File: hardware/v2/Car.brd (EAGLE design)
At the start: 83.8 x 55.9 mm, 80 parts, among them M1_CA 100n, M1_CB 100n, M1_LPF MCP6L2-X_SN, M1_LPF1 MCP6L2-X_SN, M1_R1A 105k, M1_R1B 105k, M1_R2A 200k, M1_R2B 200k, M1_RA 22k, M1_RB 22k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

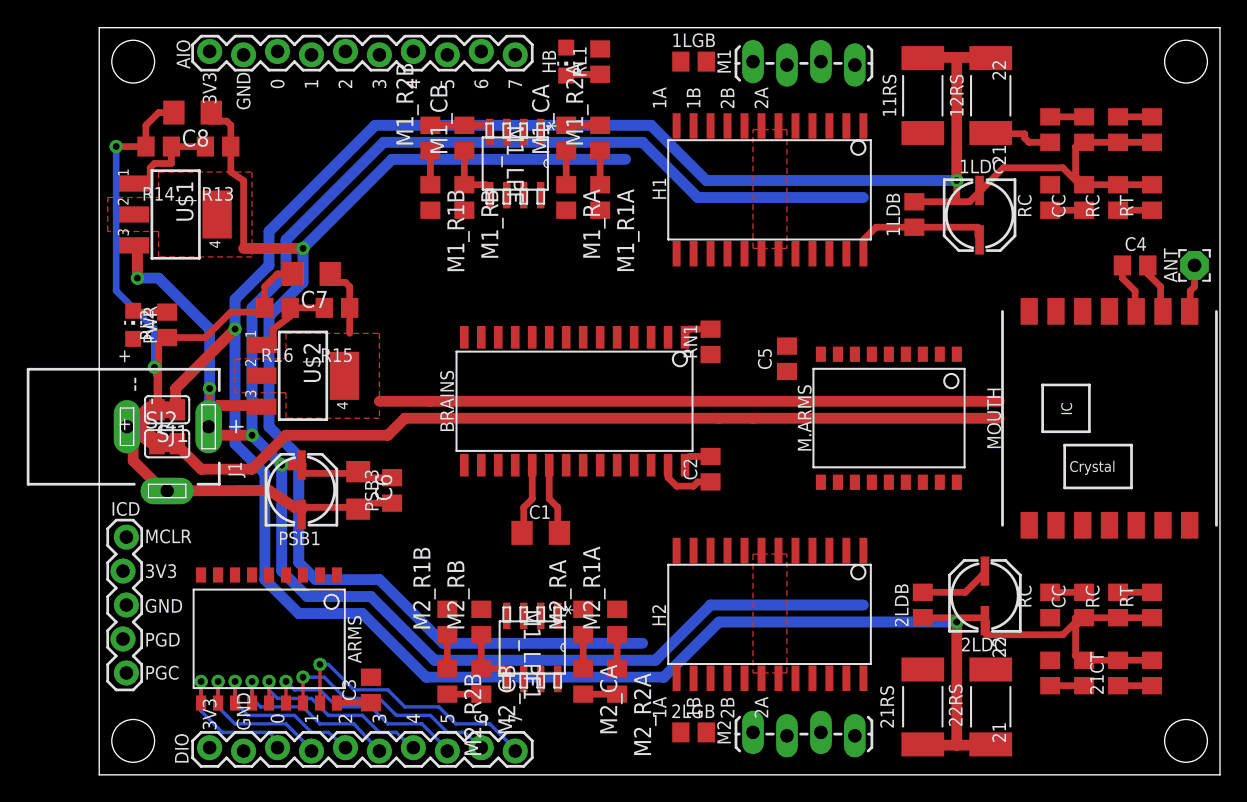
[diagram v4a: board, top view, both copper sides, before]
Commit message: Finished routing power signals.
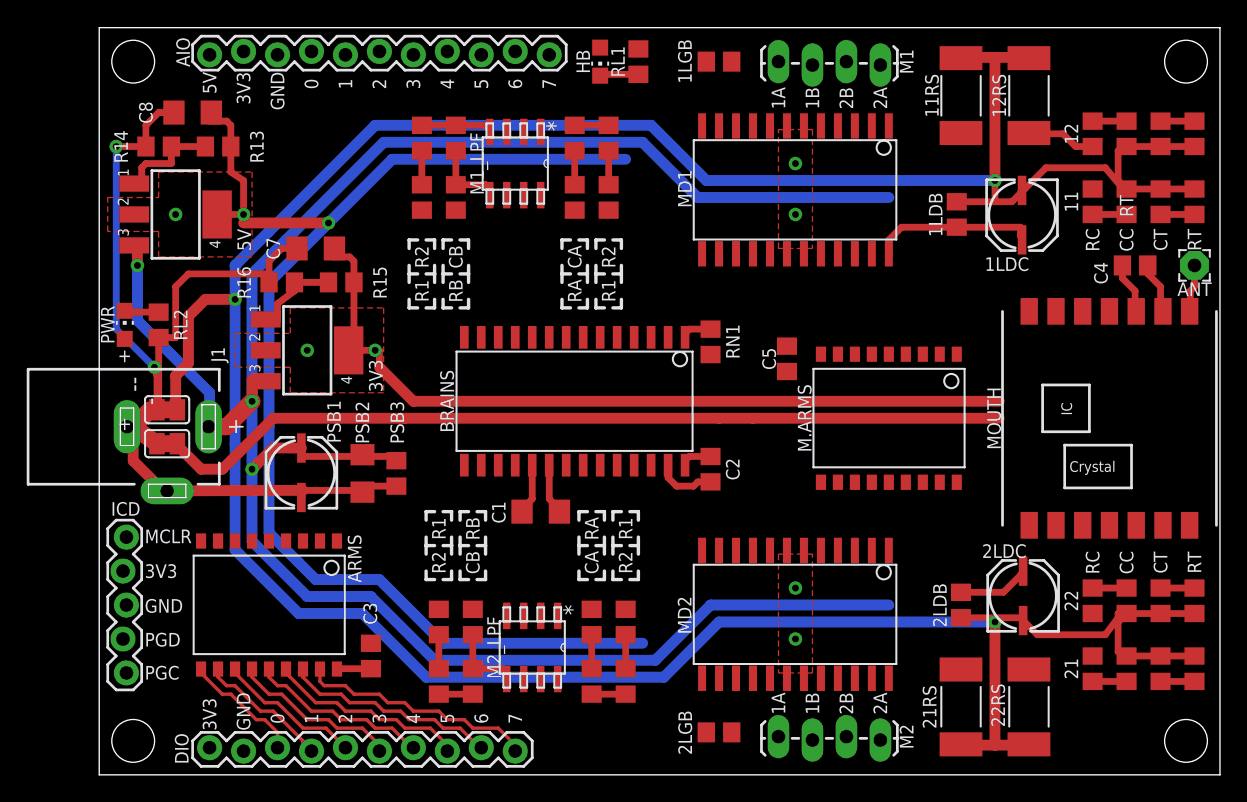
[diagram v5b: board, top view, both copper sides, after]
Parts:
- removed C6: 1u, rcl:C1206
- removed H1, H2: MTS62C19A, microchip:SOP24L
- removed U$2: LM317, misc:SOT23
- added 3V3: LM317, misc:SOT23
- added MD1, MD2: MTS62C19A, microchip:SOP24L
- added PSB2: 1u, rcl:C1206
- AIO: device SparkFun-Connectors:1X10_LOCK -> SparkFun-Connectors:1X11_LOCK
- moved AIO 25.4 mm to (33.7, 54.0), turned to 180 degrees
- moved 11RT 3.19 mm to (81.9, 42.9)
- moved 21RT 3.19 mm to (81.9, 7.94)
- moved 22RT 3.19 mm to (81.9, 13.0)
- moved 12RT 3.19 mm to (81.9, 47.9)
- moved 11CC 3.19 mm to (76.8, 42.9)
- moved 11CT 3.19 mm to (79.4, 42.9)
- moved 11RC 3.19 mm to (74.3, 42.9)
- moved 12CC 3.19 mm to (76.8, 47.9)
- moved 12CT 3.19 mm to (79.4, 47.9)
- moved 12RC 3.19 mm to (74.3, 47.9)
- moved 21CC 3.19 mm to (76.8, 7.94)
- moved 21CT 3.19 mm to (79.4, 7.94)
- moved 21RC 3.19 mm to (74.3, 7.94)
- moved 22CC 3.19 mm to (76.8, 13.0)
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- renumbered M1_LPF1 to M2_LPF, U$1 to 5V
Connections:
- net 12V: now also 3V3.3, MD1.24, MD2.24, PSB2.1; no longer C6.1, H1.24, H2.24, U$2.3
- net 3V3: now also 3V3.2, 3V3.4, AIO.10; no longer AIO.1, U$2.2, U$2.4
- net 5V: now also AIO.11, MD1.13, MD2.13; no longer H1.13, H2.13
- net A0: now also AIO.8; no longer AIO.3
- net A1: now also AIO.7; no longer AIO.4
- net A2: now also AIO.6; no longer AIO.5
- net A3: now also AIO.5; no longer AIO.6
- net A4: now also AIO.4; no longer AIO.7
- net A5: now also AIO.3; no longer AIO.8
- net A6: now also AIO.2; no longer AIO.9
- net A7: now also AIO.1; no longer AIO.10
- net DGND: now also AIO.9, MD1.18, MD1.19, MD1.6, MD1.7, MD2.18, MD2.19, MD2.6, MD2.7; no longer AIO.2, H1.18, H1.19, H1.6, H1.7, H2.18, H2.19, H2.6, H2.7
- net GND: now also PSB2.2; no longer C6.2
- net M1_I0X: now also MD1.20, MD1.8; no longer H1.20, H1.8
- net M1_I1X: now also MD1.17, MD1.9; no longer H1.17, H1.9
- net M1_P1: now also MD1.16; no longer H1.16
- net M1_P2: now also MD1.10; no longer H1.10
- net M1_V1: now also MD1.15; no longer H1.15
- net M1_V2: now also MD1.11; no longer H1.11
- net M2_I0X: now also MD2.20, MD2.8; no longer H2.20, H2.8
- net M2_I1X: now also MD2.17, MD2.9; no longer H2.17, H2.9
- net M2_P1: now also MD2.16; no longer H2.16
- net M2_P2: now also MD2.10; no longer H2.10
- net M2_V1: now also MD2.15; no longer H2.15
- net M2_V2: now also MD2.11; no longer H2.11
- net N$1: now also MD1.21; no longer H1.21
- net N$10: now also MD2.2; no longer H2.2
- net N$13: now also MD2.23; no longer H2.23
- net N$14: now also MD2.22; no longer H2.22
- net N$15: now also MD2.12; no longer H2.12
- net N$16: now also MD2.3; no longer H2.3
- net N$17: now also MD2.4; no longer H2.4
- net N$18: now also MD2.14; no longer H2.14
- net N$2: now also MD1.1; no longer H1.1
- net N$20: now also 3V3.1; no longer U$2.1
- net N$31: now also MD1.23; no longer H1.23
- net N$33: now also MD1.22; no longer H1.22
- net N$34: now also MD1.4; no longer H1.4
- net N$35: now also MD1.3; no longer H1.3
- net N$4: now also MD1.5; no longer H1.5
- net N$41: now also MD1.14; no longer H1.14
- net N$42: now also MD1.12; no longer H1.12
- net N$5: now also MD1.2; no longer H1.2
- net N$6: now also MD2.21; no longer H2.21
- net N$8: now also MD2.1; no longer H2.1
- net N$9: now also MD2.5; no longer H2.5
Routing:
- net AGND: track 251.3 -> 261.7 mm
- net 3V3: track 61.2 -> 68.9 mm, vias 0 -> 2
- net GND: track 75.4 -> 78.8 mm
- net 5V: track 97.2 -> 99.8 mm, vias 1 -> 3
- net 12V: track 177.1 -> 179.4 mm, vias 4 -> 3
- net D7: track 20.2 -> 17.9 mm, vias 1 -> 0
- net D0: track 11.0 -> 8.99 mm, vias 1 -> 0
- net D1: track 11.9 -> 9.96 mm, vias 1 -> 0
- net D2: track 12.8 -> 10.9 mm, vias 1 -> 0
- net DGND: track 77.7 -> 76.0 mm, vias 0 -> 4
- net N$40: track 5.46 -> 3.76 mm
- net D4: track 15.0 -> 13.6 mm, vias 1 -> 0
- net D3: track 14.1 -> 12.7 mm, vias 1 -> 0
- net D6: track 17.4 -> 16.1 mm, vias 1 -> 0
- net D5: track 15.9 -> 15.0 mm, vias 1 -> 0
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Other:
- board text added: "11"
- board text added: "12"
- board text added: "5V"
- board text added: "CA"
- board text added: "CB"
- board text added: "CT"
- board text added: "R1"
- board text added: "R2"
- board text added: "RA"
- board text added: "RB"

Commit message: Finalized(-ish) routing for V2
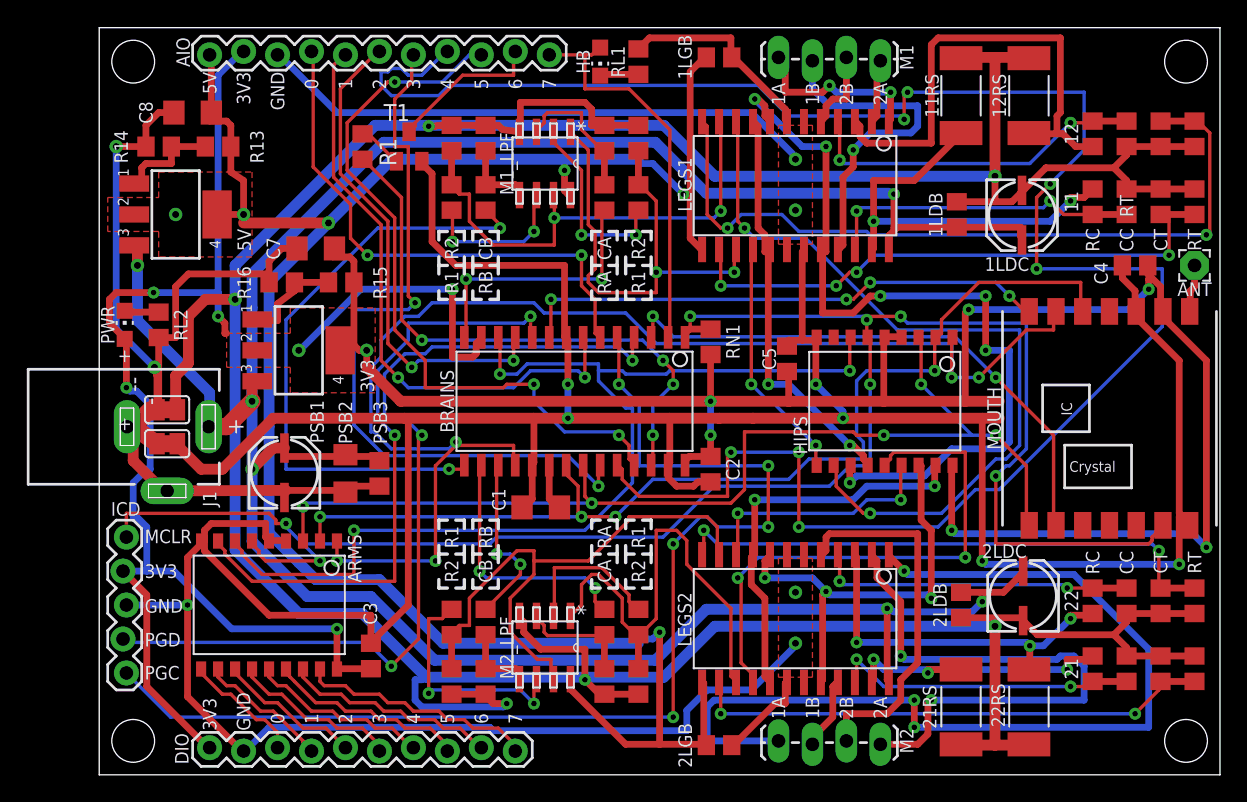
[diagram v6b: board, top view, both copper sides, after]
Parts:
- removed M.ARMS: MCP23S08, microchip:SO-18W
- removed MD1, MD2: MTS62C19A, microchip:SOP24L
- added HIPS: MCP23S08, microchip:SO-18W
- added LEGS1, LEGS2: MTS62C19A, microchip:SOP24L
- added R1: 1k, rcl:R0805
- added T1: (no value), transistor:SOT23-BEC
- moved M1_LPF 2.22 mm to (33.3, 45.7)
- moved M1_R1B 2.22 mm to (26.4, 43.2)
- moved M1_R2B 2.22 mm to (26.4, 47.6)
- moved M1_CA 2.22 mm to (37.8, 47.6)
- moved M1_CB 2.22 mm to (28.9, 47.6)
- moved M1_R1A 2.22 mm to (40.3, 43.2)
- moved M1_R2A 2.22 mm to (40.3, 47.6)
- moved M1_RA 2.22 mm to (37.8, 43.2)
- moved M1_RB 2.22 mm to (28.9, 43.2)
- moved PSB3 1.27 mm to (21.0, 22.5)
- moved PSB1 1.27 mm to (13.7, 22.5)
- moved PSB2 1.27 mm to (18.4, 22.5)
- moved M2_CA 0.95 mm to (37.8, 6.99)
- moved M2_LPF 0.95 mm to (33.3, 9.53)
- moved M2_R1A 0.95 mm to (40.3, 11.4)
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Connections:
- new net N$26: AIO.2, T1.C
- new net N$28: R1.1, T1.B
- net /RST: now also HIPS.6; no longer M.ARMS.6
- net 12V: now also LEGS1.24, LEGS2.24; no longer MD1.24, MD2.24
- net 3V3: now also HIPS.18, HIPS.4, HIPS.5; no longer M.ARMS.18, M.ARMS.4, M.ARMS.5
- net 5V: now also LEGS1.13, LEGS2.13; no longer MD1.13, MD2.13
- net A6: now also R1.2; no longer AIO.2
- net DGND: now also HIPS.9, LEGS1.18, LEGS1.19, LEGS1.6, LEGS1.7, LEGS2.18, LEGS2.19, LEGS2.6, LEGS2.7, T1.E; no longer M.ARMS.9, MD1.18, MD1.19, MD1.6, MD1.7, MD2.18, MD2.19, MD2.6, MD2.7
- net DIO_CS: now also HIPS.7; no longer M.ARMS.7
- net M1_I0X: now also HIPS.12, LEGS1.20, LEGS1.8; no longer M.ARMS.12, MD1.20, MD1.8
- net M1_I1X: now also HIPS.13, LEGS1.17, LEGS1.9; no longer M.ARMS.13, MD1.17, MD1.9
- net M1_P1: now also HIPS.10, LEGS1.16; no longer M.ARMS.10, MD1.16
- net M1_P2: now also HIPS.11, LEGS1.10; no longer M.ARMS.11, MD1.10
- net M1_V1: now also LEGS1.15; no longer MD1.15
- net M1_V2: now also LEGS1.11; no longer MD1.11
- net M2_I0X: now also HIPS.16, LEGS2.20, LEGS2.8; no longer M.ARMS.16, MD2.20, MD2.8
- net M2_I1X: now also HIPS.17, LEGS2.17, LEGS2.9; no longer M.ARMS.17, MD2.17, MD2.9
- net M2_P1: now also HIPS.14, LEGS2.16; no longer M.ARMS.14, MD2.16
- net M2_P2: now also HIPS.15, LEGS2.10; no longer M.ARMS.15, MD2.10
- net M2_V1: now also LEGS2.15; no longer MD2.15
- net M2_V2: now also LEGS2.11; no longer MD2.11
- net MISO: now also HIPS.3; no longer M.ARMS.3
- net MOSI: now also HIPS.2; no longer M.ARMS.2
- net N$1: now also LEGS1.21; no longer MD1.21
- net N$10: now also LEGS2.2; no longer MD2.2
- net N$13: now also LEGS2.23; no longer MD2.23
- net N$14: now also LEGS2.22; no longer MD2.22
- net N$15: now also LEGS2.12; no longer MD2.12
- net N$16: now also LEGS2.3; no longer MD2.3
- net N$17: now also LEGS2.4; no longer MD2.4
- net N$18: now also LEGS2.14; no longer MD2.14
- net N$2: now also LEGS1.1; no longer MD1.1
- net N$31: now also LEGS1.23; no longer MD1.23
- net N$33: now also LEGS1.22; no longer MD1.22
- net N$34: now also LEGS1.4; no longer MD1.4
- net N$35: now also LEGS1.3; no longer MD1.3
- net N$4: now also LEGS1.5; no longer MD1.5
- net N$41: now also LEGS1.14; no longer MD1.14
- net N$42: now also LEGS1.12; no longer MD1.12
- net N$5: now also LEGS1.2; no longer MD1.2
- net N$6: now also LEGS2.21; no longer MD2.21
- net N$8: now also LEGS2.1; no longer MD2.1
- net N$9: now also LEGS2.5; no longer MD2.5
- net SCLK: now also HIPS.1; no longer M.ARMS.1
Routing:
- net DGND: track 76.0 -> 351.6 mm, vias 4 -> 11
- net 3V3: track 68.9 -> 263.2 mm, vias 2 -> 13
- net A4: track 0.00 -> 148.7 mm, vias 0 -> 7
- net /RST: track 2.34 -> 139.6 mm, vias 0 -> 7
- net SCLK: track 0.00 -> 99.7 mm, vias 0 -> 5
- net PGC: track 0.00 -> 88.0 mm, vias 0 -> 5
- net MISO: track 0.00 -> 79.3 mm, vias 0 -> 5
- net MOSI: track 0.00 -> 78.7 mm, vias 0 -> 4
- net DIO_CS: track 0.00 -> 78.0 mm, vias 0 -> 3
- net N$8: track 0.00 -> 71.4 mm, vias 0 -> 3
- net PGD: track 0.00 -> 67.2 mm, vias 0 -> 3
- net M1_I0X: track 0.00 -> 62.0 mm, vias 0 -> 6
- net M1_P2: track 0.00 -> 59.0 mm, vias 0 -> 2
- net 5V: track 99.8 -> 156.2 mm, vias 3 -> 6
- net A3: track 0.00 -> 55.7 mm, vias 0 -> 2
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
